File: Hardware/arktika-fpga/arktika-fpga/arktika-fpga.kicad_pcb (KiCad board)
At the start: 4 copper layers, 133.2 x 81.3 mm, 135 parts

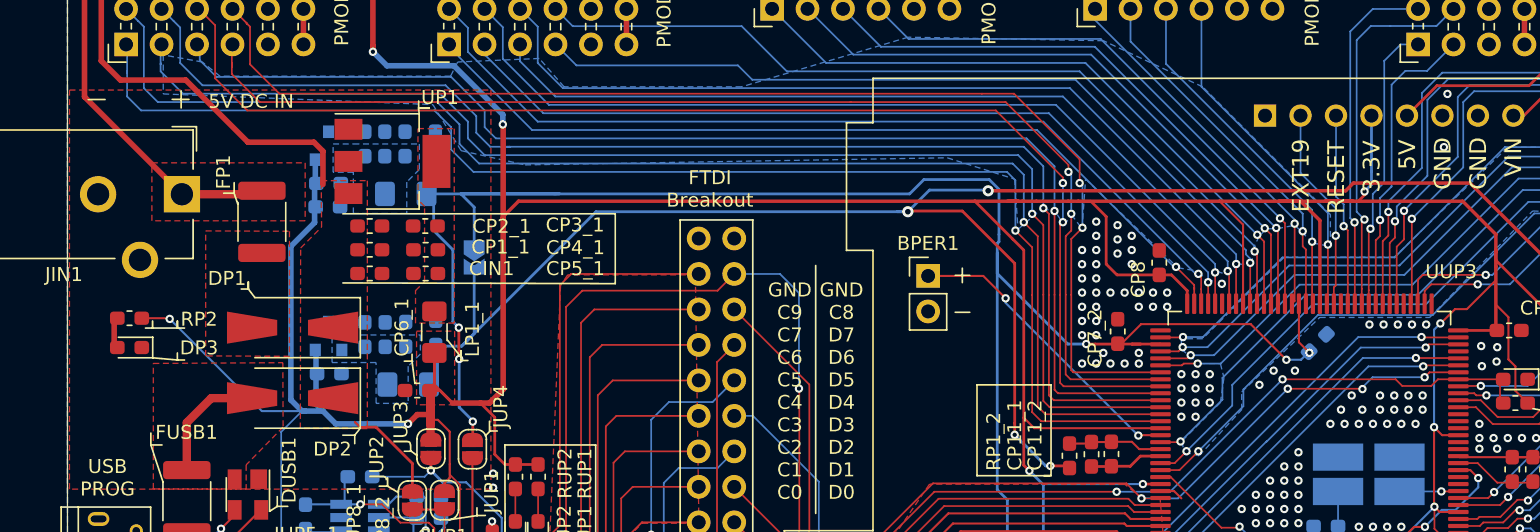
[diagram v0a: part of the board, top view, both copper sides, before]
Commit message: Added silkscreen art and added media folder with the same art
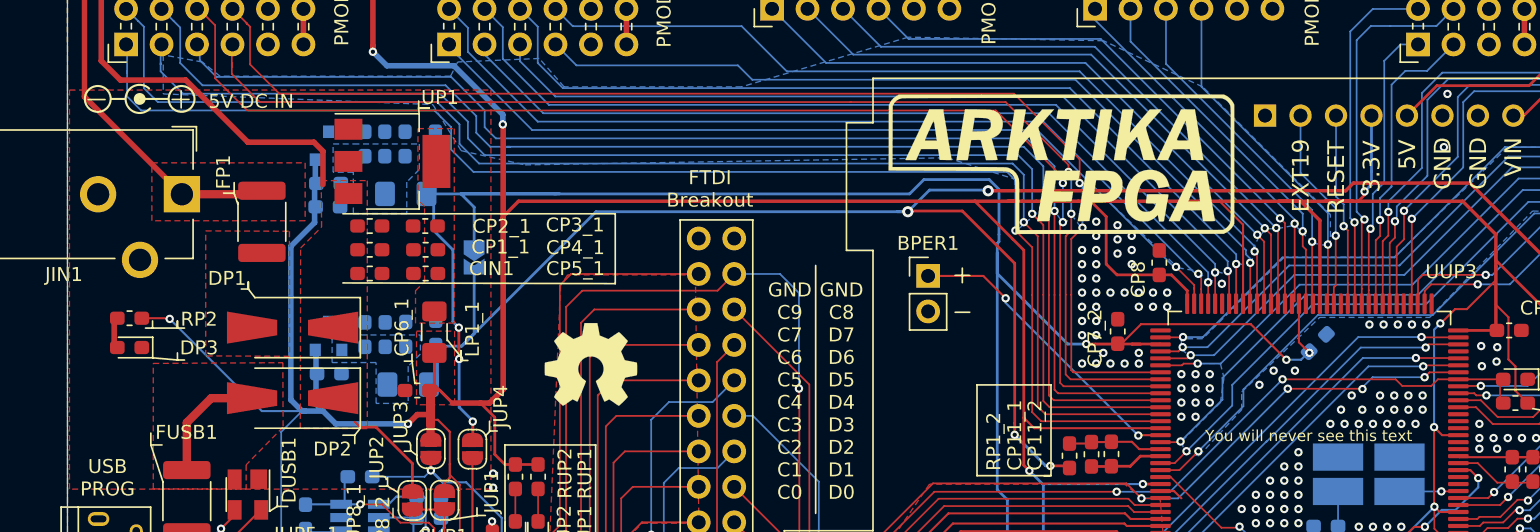
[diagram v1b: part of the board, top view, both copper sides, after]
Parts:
- added G***: LOGO, Arktica-Specific:arktika-fpga-logo-smaller, F.Cu at (155.2, 73.7)
- added G***: LOGO, Arktica-Specific:arktika-fpga-logo, B.Cu at (151.8, 73.5)
- added REF**: OSHW-Symbol_6.7x6mm_SilkScreen, Symbol:OSHW-Symbol_6.7x6mm_SilkScreen, F.Cu at (121.8, 87.2)
- added REF**: Symbol_Barrel_Polarity, Symbol:Symbol_Barrel_Polarity, F.Cu at (89.5, 68.1)
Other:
- board text added: "Ice cap miles thaw to freedom Sets free the Antarctic legion Awake limbs, to reach a sun's rays Blood thaws troughout the unused veins"
- board text added: "You will never see this text"

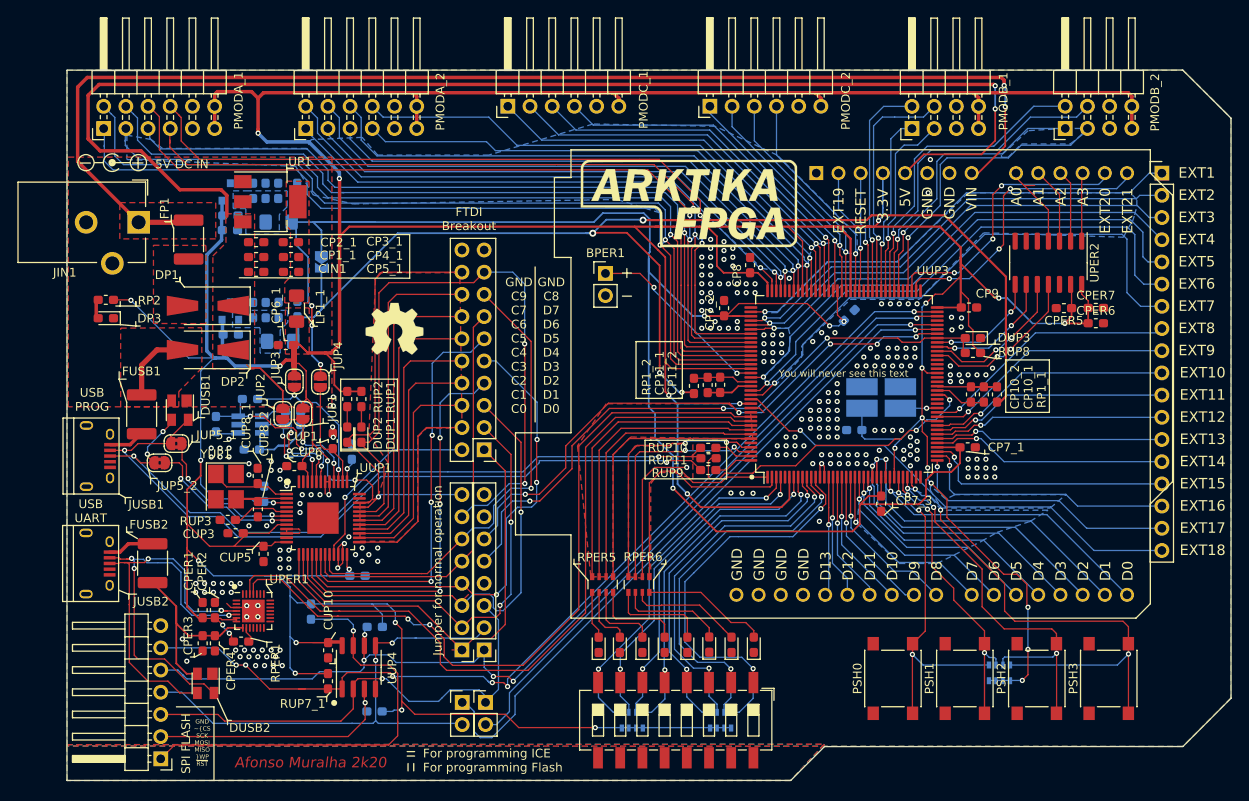
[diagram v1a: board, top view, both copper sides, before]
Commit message: Minor layout fixes. Added new micro usb connector footprint and link. Misc silk changes
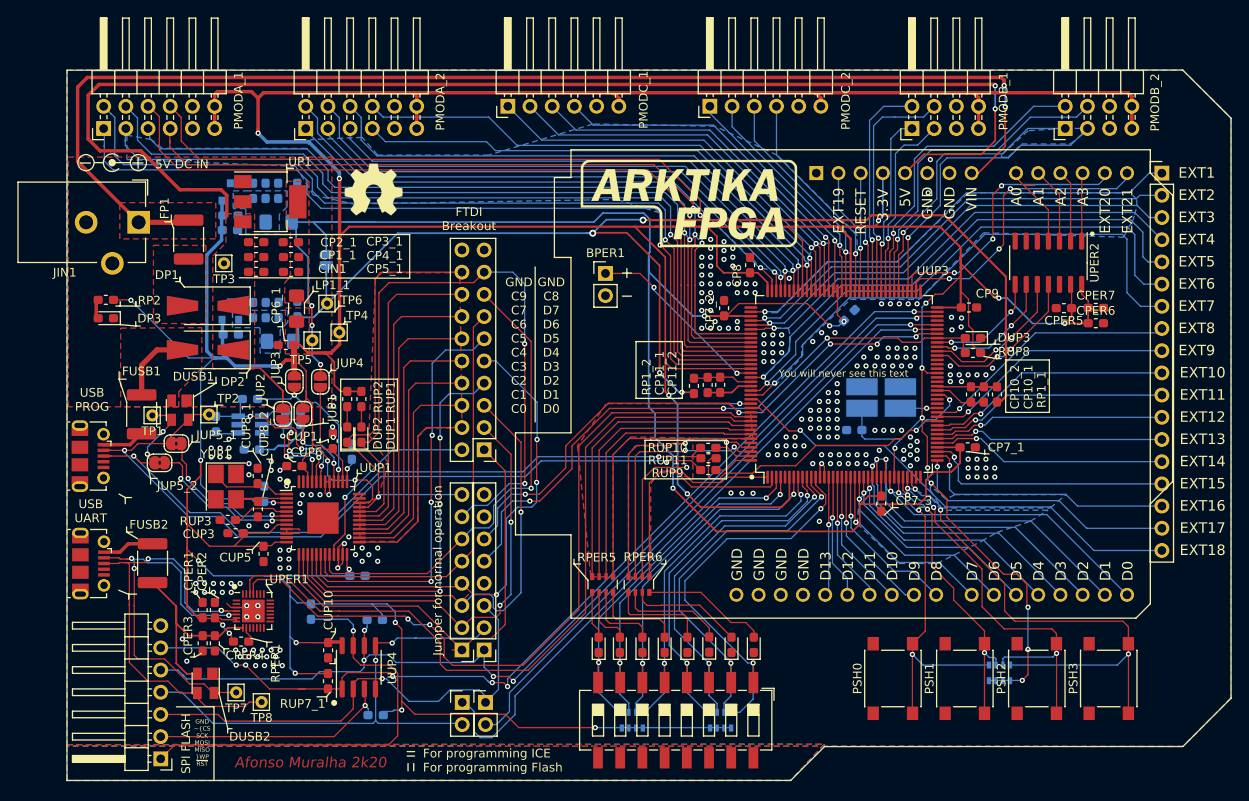
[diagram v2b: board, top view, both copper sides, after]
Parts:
- added TP1: TestPoint, Connector_Pin:Pin_D0.7mm_L6.5mm_W1.8mm_FlatFork, F.Cu at (94.1, 97.1)
- added TP2: TestPoint, Connector_Pin:Pin_D0.7mm_L6.5mm_W1.8mm_FlatFork, F.Cu at (100.6, 97.0)
- added TP3: TestPoint, Connector_Pin:Pin_D0.7mm_L6.5mm_W1.8mm_FlatFork, F.Cu at (102.3, 79.7)
- added TP4: TestPoint, Connector_Pin:Pin_D0.7mm_L6.5mm_W1.8mm_FlatFork, F.Cu at (115.5, 87.6)
- added TP5: TestPoint, Connector_Pin:Pin_D0.7mm_L6.5mm_W1.8mm_FlatFork, F.Cu at (112.4, 88.5)
- added TP6: TestPoint, Connector_Pin:Pin_D0.7mm_L6.5mm_W1.8mm_FlatFork, F.Cu at (114.1, 84.3)
- added TP7: TestPoint, Connector_Pin:Pin_D0.7mm_L6.5mm_W1.8mm_FlatFork, F.Cu at (103.7, 128.8)
- added TP8: TestPoint, Connector_Pin:Pin_D0.7mm_L6.5mm_W1.8mm_FlatFork, F.Cu at (106.6, 129.9)
- JP2: footprint Jumper:SolderJumper-2_P1.3mm_Open_TrianglePad1.0x1.5mm -> Jumper:SolderJumper-2_P1.3mm_Open_RoundedPad1.0x1.5mm
- JUSB1, JUSB2: footprint Connectors:USB_Micro-B -> Connector_USB:USB_Micro-B_Molex-105017-0001
- moved G*** 36.0 mm to (151.8, 109.5)
- moved REF** 16.1 mm to (119.4, 71.3)
- moved JUSB1 0.86 mm to (87.0, 101.8)
- moved RUP7_4 0.80 mm to (119.5, 120.5)
- moved JUSB2 0.76 mm to (87.1, 114.0)
- moved JP2 0.59 mm to (114.0, 79.3)
- moved RUP7_2 0.44 mm to (119.7, 131.4)
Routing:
- net /FPGA_PERIPHS/D+: track 45.9 -> 54.5 mm
- net /D-: track 85.5 -> 88.8 mm
- net /D+: track 85.4 -> 88.3 mm
- net /FPGA_PERIPHS/D-: track 42.4 -> 45.0 mm
- net /FPGA_IO/SW0: track 47.5 -> 45.8 mm
- net /FPGA_IO/SW1: track 44.7 -> 43.2 mm
- net Net-(FUSB1-Pad2): track 4.60 -> 5.56 mm
- net /FPGA_IO/SW2: track 43.0 -> 42.2 mm
- net /USB AND PROG/ICE_SCK: track 116.4 -> 117.2 mm
- net /VCC3V3: track 762.2 -> 761.4 mm
- net /FPGA_IO/SW6: track 39.9 -> 40.7 mm
- net /Power/VCC1.2_PLL: track 139.9 -> 140.7 mm
- net /USB AND PROG/flash_~WP: track 28.9 -> 28.2 mm
- net /FPGA_IO/SW5: track 39.9 -> 40.5 mm

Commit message: Added pcbway logo to top silkscreen
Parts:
- added G***: LOGO, Arktica-Specific:pcbway_smallerer, F.Cu at (126.0, 70.3)
- moved REF** 16.2 mm to (123.3, 87.0)

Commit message: misc changes, exported test gerbers
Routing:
- net /FPGA_PERIPHS/D+: track 54.5 -> 50.8 mm
- net /FPGA_PERIPHS/D-: track 45.0 -> 44.5 mm
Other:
- copper layers 4 -> 2
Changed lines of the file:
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@@
     (thickness 1.6002)
     (drawings 320)
-    (tracks 2629)
+    (tracks 2624)
     (zones 0)
     (modules 148)
@@
   (title_block
     (title "Arktica FPGA")
+    (date 2020-08-04)
     (company "Authors: Afonso Muralha and João Nuno Carvalho")
   )
   (layers
     (0 Front signal)
-    (1 In1.Cu signal hide)
-    (2 In2.Cu signal hide)
     (31 Back signal)
     (34 B.Paste user)
-    (35 F.Paste user hide)
+    (35 F.Paste user)
     (36 B.SilkS user)
     (37 F.SilkS user)
@@
     (45 Margin user)
     (46 B.CrtYd user)
-    (47 F.CrtYd user hide)
+    (47 F.CrtYd user)
     (49 F.Fab user)
   )
@@
     (visible_elements 7FFFFF7F)
     (pcbplotparams
-      (layerselection 0x01054_fffffff8)
-      (usegerberextensions false)
+      (layerselection 0x030fc_ffffffff)
+      (usegerberextensions true)
       (usegerberattributes true)
       (usegerberadvancedattributes true)
@@
       (padsonsilk false)
       (subtractmaskfromsilk false)
-      (outputformat 3)
+      (outputformat 1)
       (mirror false)
       (drillshape 0)
       (scaleselection 1)
-      (outputdirectory ""))
+      (outputdirectory "Outputs/GERBERs/"))
   )
   (net 0 "")
@@
   (segment (start 90.8795 113.943) (end 93.1925 113.943) (width 0.125) (layer Front) (net 52))
   (segment (start 93.1925 113.943) (end 93.21725 113.91825) (width 0.125) (layer Front) (net 52))
-  (segment (start 102.329779 119.5295) (end 101.47927 120.380009) (width 0.125) (layer In2.Cu) (net 52))
-  (segment (start 102 119.859279) (end 102 119.42) (width 0.125) (layer In2.Cu) (net 52))
   (segment (start 101.7505 119.4795) (end 101.81 119.42) (width 0.125) (layer Front) (net 52))
   (segment (start 102.678743 119.4795) (end 101.7505 119.4795) (width 0.125) (layer Front) (net 52))
-  (segment (start 101.47927 120.380009) (end 102 119.859279) (width 0.125) (layer In2.Cu) (net 52))
   (segment (start 103.7055 119.4795) (end 101.7505 119.4795) (width 0.125) (layer Front) (net 52))
-  (segment (start 102.379779 119.4795) (end 101.47927 120.380009) (width 0.125) (layer In2.Cu) (net 52))
   (via (at 102 119.42) (size 0.6) (drill 0.3) (layers Front Back) (net 52))
   (segment (start 101.81 119.42) (end 102 119.42) (width 0.125) (layer Front) (net 52))
@@
   (segment (start 94.72 113.9605) (end 96.3068 113.9605) (width 0.125) (layer Back) (net 53))
   (segment (start 93.475 113.9605) (end 94.72 113.9605) (width 0.125) (layer Back) (net 53))
-  (segment (start 102.329779 119.9795) (end 102.8595 119.9795) (width 0.2) (layer In2.Cu) (net 53))
   (via (at 102.8595 119.9795) (size 0.6) (drill 0.3) (layers Front Back) (net 53))
   (segment (start 102.5555 119.9795) (end 102.8595 119.9795) (width 0.125) (layer Back) (net 53))
